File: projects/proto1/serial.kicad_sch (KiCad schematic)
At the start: 15 parts, among them J4 5747840-4, J5 5747840-4, U18 MAX232, U19 74LS00, U20 MC68681P, U21 MAX232

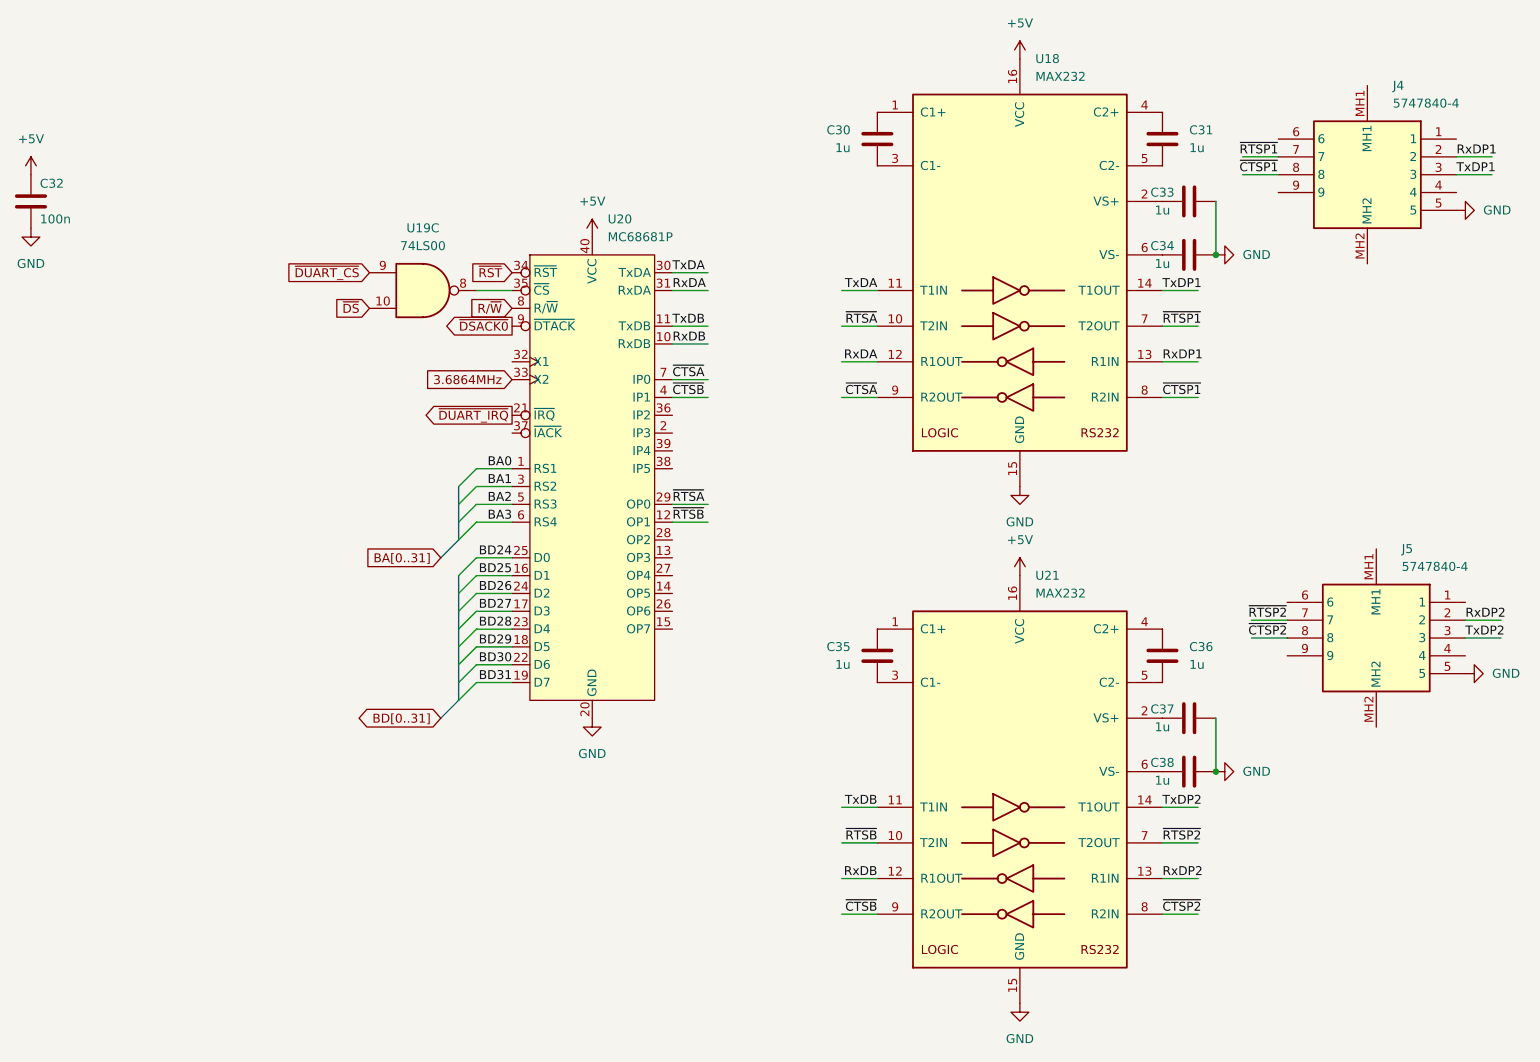
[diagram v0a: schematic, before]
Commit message: Renamed CMC to SCU, changed verification method to cocotb, and modified pcb schematic
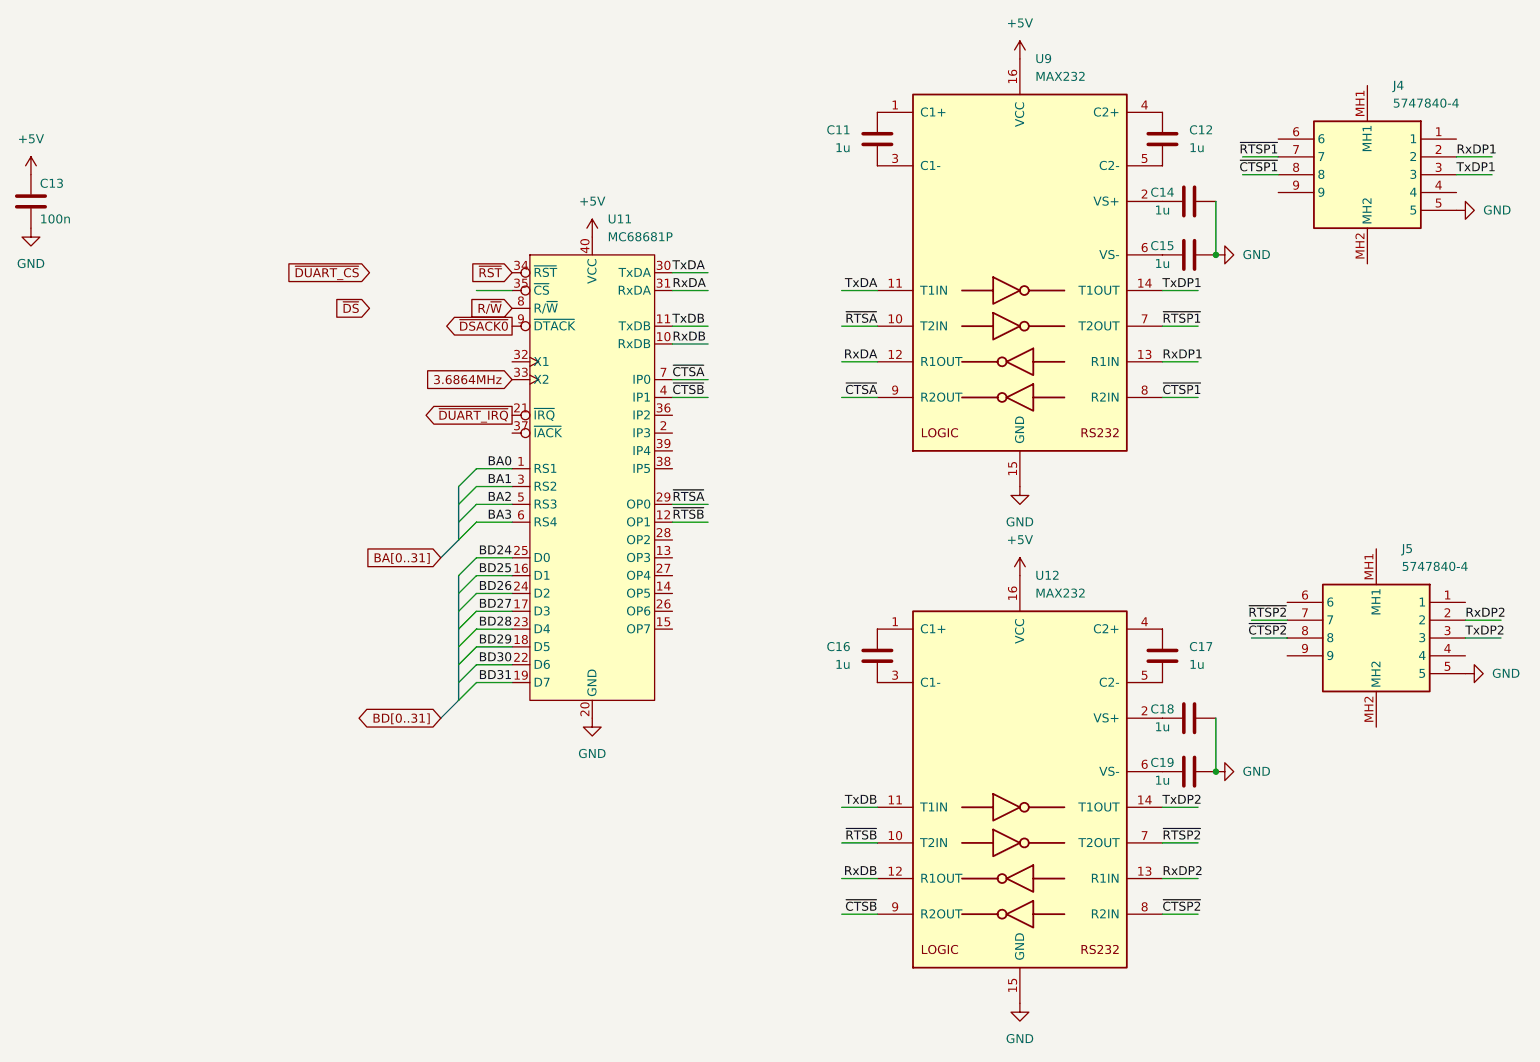
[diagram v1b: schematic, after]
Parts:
- removed U19: 74LS00, Package_DIP:DIP-14_W7.62mm_Socket, symbol 74xx:74LS00
- renumbered C30 to C11, C31 to C12, C32 to C13, C33 to C14, C34 to C15, C35 to C16, C36 to C17, C37 to C18, C38 to C19, U20 to U11, U21 to U12, U18 to U9
